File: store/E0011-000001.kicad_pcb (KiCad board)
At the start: 2 copper layers, 147 x 55 mm, 146 parts, among them J1 Sensor_Header_A, J10 U3 U4 1-Wire, J11 RT2 lead, J12 SF1 flow switch, J13 E6 valve, J14 expansion, J15 RT3 RT4 leads, J2 Sensor_Header_B, J3 +24V in, J4 E1 to E0012, J5 fan E2, J6 E0012 sensing, J7 E3 subcooler, J8 E4 reheater, J9 fan E5, Q1 2N7002, Q2 2N7002, Q3 TBD, Q4 TBD, U10 M24C64, U11 SN74LVC08AD, U5 DRV8262DDW, U6 DRV8262DDW, U7 MCP6567, U8 MCP6569, U9 PCA9685PW

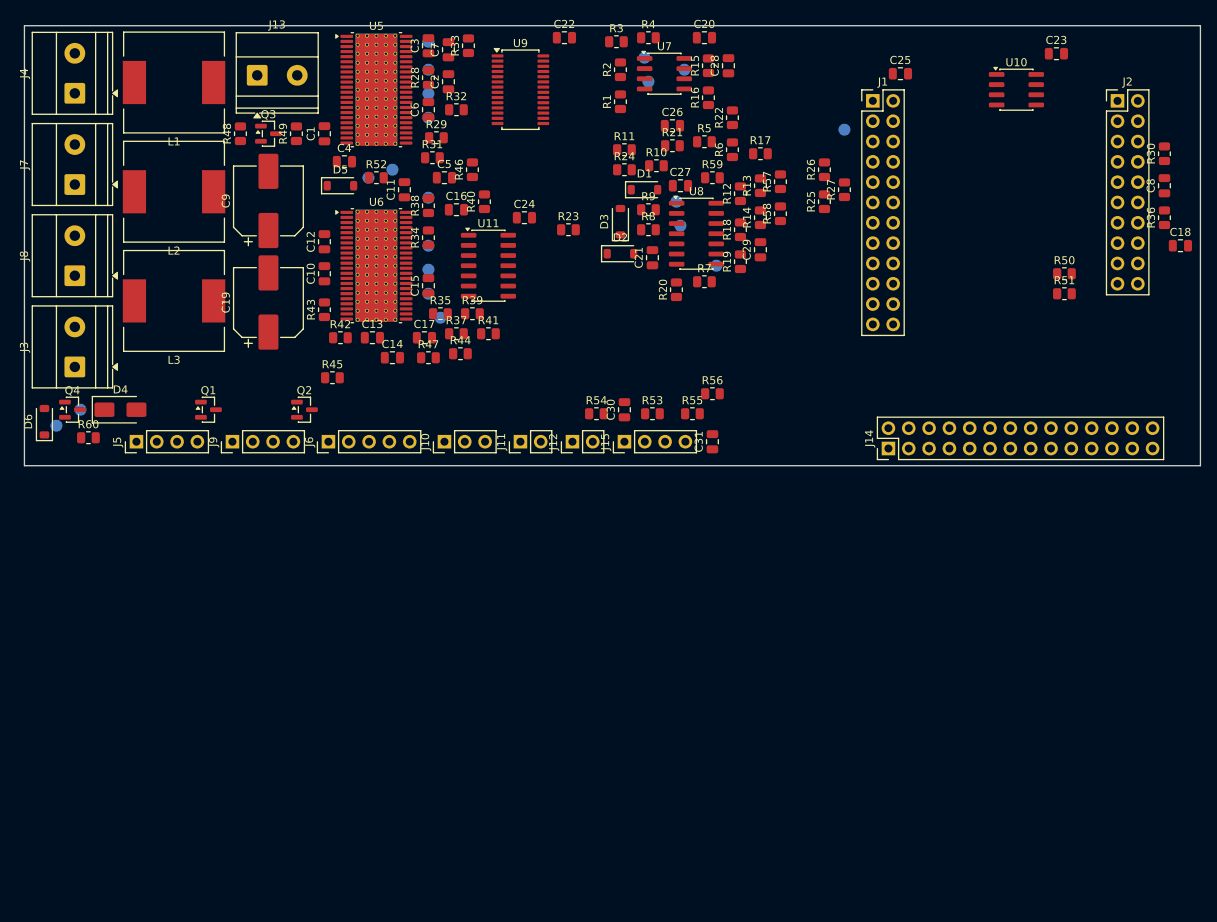
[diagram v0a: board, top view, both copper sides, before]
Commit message: E0011: board outline and placement
The outline carries four corner mounting holes and a carrier footprint
centred between two connector strips. Signal headers occupy one long edge
and power terminals the other, their wire entry facing off the board. Each
driver sits at the carrier band's lower edge above its bulk capacitor,
output inductor and terminal. Interlock sensing, the fan drives and the
spare thermistor channels occupy the signal strip. Connectivity is
unchanged and silkscreen clearance is clean.

Signed-off-by: IIchukissII <133657307+IIchukissII@users.noreply.github.com>
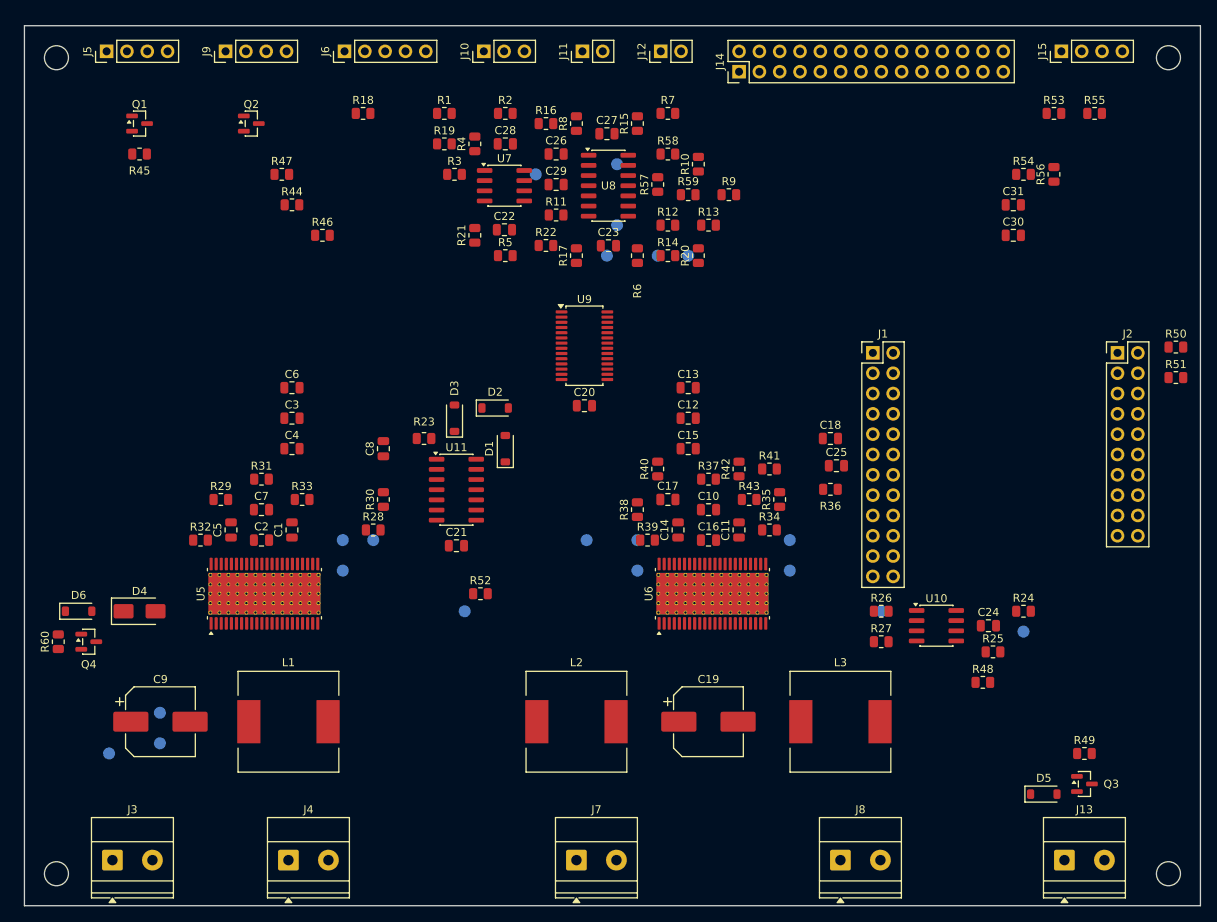
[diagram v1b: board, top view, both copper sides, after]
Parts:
- moved J13 140.7 mm to (188.0, 154.3)
- moved Q3 130.4 mm to (190.5, 144.8)
- moved R49 125.3 mm to (190.5, 141.0), turned to 0 degrees
- moved J8 120.4 mm to (160.0, 154.3), turned to 0 degrees
- moved D5 116.2 mm to (185.4, 146.0)
- moved R48 115.4 mm to (177.8, 132.1), turned to 0 degrees
- moved R30 106.8 mm to (102.9, 109.2)
- moved J7 105.2 mm to (127.0, 154.3), turned to 0 degrees
- moved C8 103.0 mm to (102.9, 102.9)
- moved J4 99.5 mm to (91.0, 154.3), turned to 0 degrees
- moved L3 98.5 mm to (160.0, 137.0), turned to 0 degrees
- moved TP14 83.7 mm to (165.1, 123.2)
- moved L2 83.2 mm to (127.0, 137.0), turned to 0 degrees
- moved L1 81.2 mm to (91.0, 137.0), turned to 0 degrees
- moved TP2 77.4 mm to (74.9, 139.7)
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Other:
- board size 147 x 55 mm -> 147 x 110 mm

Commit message: E0011: latching connectors on the field leads
The seven sensing and fan leads carry Micro-Fit 3.0 horizontal headers, whose
latch and through-hole tails retain the mating connector. Every 24 V lead now
leaves the board on the terminal edge and the opposite edge carries sensing
only. Circuit counts, net membership and the unconnected count are unchanged.

Signed-off-by: IIchukissII <133657307+IIchukissII@users.noreply.github.com>
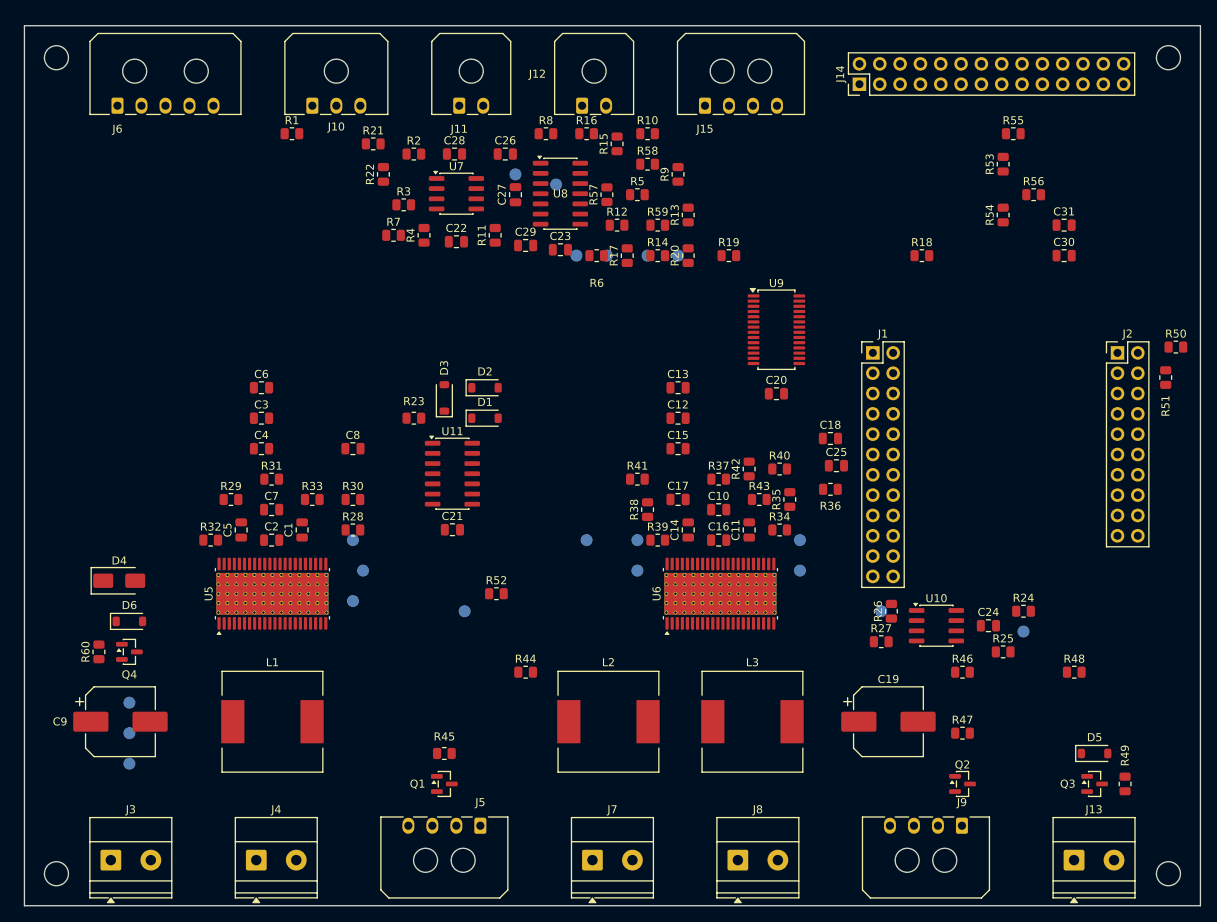
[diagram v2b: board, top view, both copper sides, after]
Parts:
- J10: footprint Connector_PinHeader_2.54mm:PinHeader_1x03_P2.54mm_Vertical -> Connector_Molex:Molex_Micro-Fit_3.0_43650-0300_1x03_P3.00mm_Horizontal
- J11, J12: footprint Connector_PinHeader_2.54mm:PinHeader_1x02_P2.54mm_Vertical -> Connector_Molex:Molex_Micro-Fit_3.0_43650-0200_1x02_P3.00mm_Horizontal
- J15, J5, J9: footprint Connector_PinHeader_2.54mm:PinHeader_1x04_P2.54mm_Vertical -> Connector_Molex:Molex_Micro-Fit_3.0_43650-0400_1x04_P3.00mm_Horizontal
- J6: footprint Connector_PinHeader_2.54mm:PinHeader_1x05_P2.54mm_Vertical -> Connector_Molex:Molex_Micro-Fit_3.0_43650-0500_1x05_P3.00mm_Horizontal
- moved J9 133.6 mm to (175.2, 150.0), turned to 180 degrees
- moved Q2 121.3 mm to (175.3, 144.8)
- moved R47 110.1 mm to (175.3, 138.4)
- moved J5 107.5 mm to (115.0, 150.0), turned to 180 degrees
- moved R46 96.9 mm to (175.3, 130.8)
- moved Q1 90.9 mm to (110.5, 144.8)
- moved R45 84.1 mm to (110.5, 141.0)
- moved R18 72.1 mm to (170.2, 78.7)
- moved R44 65.3 mm to (120.6, 130.8)
- moved J15 45.1 mm to (143.1, 60.0), turned to 0 degrees
- moved R19 38.2 mm to (146.1, 78.7)
- moved R7 37.5 mm to (104.1, 76.2)
- moved J6 29.2 mm to (69.6, 60.0), turned to 0 degrees
- moved U9 24.1 mm to (152.0, 88.0)
- moved C20 24.0 mm to (152.0, 96.0)
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
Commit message: E0011: placement revised
Footprints move toward their final positions within the existing outline.
The placement is incomplete and the board remains unrouted. Net membership
and the unconnected count are unchanged.

Signed-off-by: IIchukissII <133657307+IIchukissII@users.noreply.github.com>
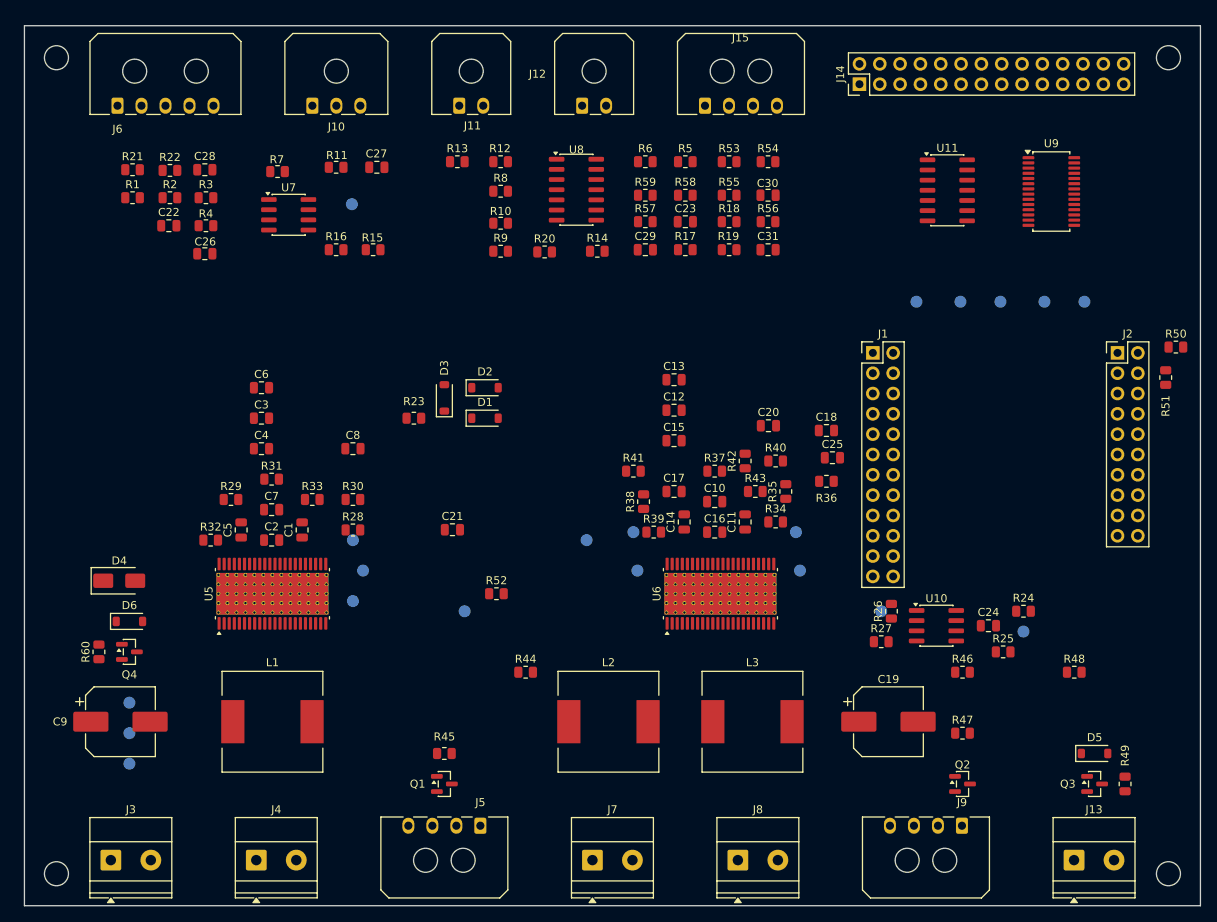
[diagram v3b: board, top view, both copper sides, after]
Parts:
- moved U11 71.3 mm to (173.4, 70.6)
- moved TP16 51.1 mm to (190.5, 84.5)
- moved TP18 49.9 mm to (185.5, 84.5)
- moved TP17 49.5 mm to (180.0, 84.5)
- moved TP15 48.3 mm to (175.0, 84.5)
- moved TP20 47.4 mm to (169.5, 84.5)
- moved C26 39.6 mm to (80.5, 78.5), turned to 180 degrees
- moved U9 38.5 mm to (186.4, 70.7)
- moved C30 37.8 mm to (150.9, 71.2), turned to 180 degrees
- moved C31 37.1 mm to (150.9, 78.0), turned to 180 degrees
- moved R55 36.3 mm to (146.1, 71.2)
- moved C22 36.0 mm to (76.0, 75.0)
- moved R16 34.5 mm to (97.0, 78.0)
- moved R53 34.3 mm to (146.1, 67.0), turned to 180 degrees
- moved R56 33.4 mm to (150.9, 74.5)
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
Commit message: E0011: logic-band placement revised
Passives, diodes, transistors and test points across the logic band and
the driver row take new positions, along with four of the small
integrated circuits.

Connectivity, footprints and values are untouched, schematic parity is
clean, and the design rule check reports silkscreen warnings only.

Support parts of both drivers still sit away from the pins they serve.
That band holds no free room, so closing it needs the band reorganised
rather than parts moved one at a time.

Signed-off-by: IIchukissII <133657307+IIchukissII@users.noreply.github.com>
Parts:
- moved R48 59.8 mm to (181.6, 71.5), turned to 180 degrees
- moved R46 55.7 mm to (181.6, 75.5), turned to 180 degrees
- moved TP13 45.0 mm to (162.0, 84.5)
- moved R49 43.2 mm to (180.1, 104.5), turned to 180 degrees
- moved TP8 38.7 mm to (117.5, 108.5)
- moved D3 37.2 mm to (145.8, 85.0), turned to 0 degrees
- moved TP3 36.7 mm to (146.5, 121.0)
- moved Q3 36.6 mm to (180.2, 110.1), turned to -90 degrees
- moved C24 33.5 mm to (184.1, 92.0)
- moved U10 31.7 mm to (178.0, 93.9)
- moved R24 31.5 mm to (188.0, 92.1)
- moved D5 27.9 mm to (180.3, 115.5)
- moved D1 26.3 mm to (137.8, 85.0)
- moved R40 25.2 mm to (126.7, 105.0)
- moved R25 24.2 mm to (175.6, 104.5)
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
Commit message: E0011: control-band passives on 0603, support parts moved, inner planes added
Signed-off-by: IIchukissII <133657307+IIchukissII@users.noreply.github.com>
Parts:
- C11: footprint Capacitor_SMD:C_0805_2012Metric -> Capacitor_SMD:C_0603_1608Metric
- R29, R30, R31, R32, R33, R34, R35, R36, R37, R38, R39, R40, R41, R42: footprint Resistor_SMD:R_0805_2012Metric -> Resistor_SMD:R_0603_1608Metric
- moved R33 17.6 mm to (78.0, 100.0), turned to 90 degrees
- moved C2 4.47 mm to (71.4, 101.0), turned to 90 degrees
- moved C11 3.63 mm to (129.9, 100.9), turned to 90 degrees
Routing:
- added copper zone on In2.Cu, net GND
- added copper zone on In1.Cu, net GNDPWR
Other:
- copper layers 2 -> 4

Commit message: E0011: board routed
Signed-off-by: IIchukissII <133657307+IIchukissII@users.noreply.github.com>
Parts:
- moved C11 2.37 mm to (129.5, 103.2)
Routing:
- net +3.3V: track 0.00 -> 668.2 mm, vias 0 -> 1
- net +24V: track 0.00 -> 396.0 mm, vias 0 -> 11
- net T2_N: track 0.00 -> 178.8 mm, vias 0 -> 7
- net T4_N: track 0.00 -> 167.3 mm, vias 0 -> 6
- net nFAULT: track 0.00 -> 163.5 mm, vias 0 -> 7
- net T3_N: track 0.00 -> 155.0 mm, vias 0 -> 10
- net ADC_3: track 0.00 -> 153.2 mm, vias 0 -> 2
- net GND: track 0.00 -> 151.8 mm, vias 0 -> 64
- net OW_DATA: track 0.00 -> 151.2 mm, vias 0 -> 5
- net E2_PWM: track 0.00 -> 144.8 mm, vias 0 -> 2
- net T5_N: track 0.00 -> 144.1 mm, vias 0 -> 4
- net E1_PH: track 0.00 -> 132.7 mm, vias 0 -> 2
- net ADC_1: track 0.00 -> 120.2 mm, vias 0 -> 2
- net nSLEEP_U5: track 0.00 -> 115.3 mm, vias 0 -> 2
- net PWM_1: track 0.00 -> 111.0 mm, vias 0 -> 4
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- added copper zone on F.Cu, net GND
